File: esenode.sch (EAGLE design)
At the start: 11 parts, among them Q1 CSTCR6M00G53Z, U1 LPC11U6XJBD48, U2 RFM95W-868S2

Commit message: #challenge, then connect gpio to top bar and see if still possible lol
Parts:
- removed LD1: 67-23SDRSUGSUBC/TR8, everlight:67-23SDRSUGSUBC/TR8
- removed R3, R4: 10, eagle-ltspice:RR0603
- removed U2: RFM95W-868S2, RFM95W-868S2:RFM95W-868S2
- added C1: 1U, rcl:C-EUC0805
- added S1, S2: DTSM-6, switch-tact:DTSM-6
- added SV1, SV3: (no value), con-lstb:MA09-1
- added SV2: (no value), con-lstb:MA12-1
- R1: value 1U -> 10k; device resistor:R-EU_R0603 -> rcl:R-EU_M0805
- R2: value 56 -> 10k; device eagle-ltspice:RR0603 -> rcl:R-EU_M0805
- U1: value LPC11U6XJBD48 -> LPC11U68JBD64; device NXP_60_26022015:LPC11U6XJBD48 -> NXP_60_26022015:LPC11U68JBD64
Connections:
- net N$1 renamed XIN
- net N$2 renamed XOUT
- net N$3 renamed D-
- net N$4 renamed D+
- net N$5 renamed VIN
- removed net +3V3: LD1.CA, R1.1, U$2.VOUT, U$3.VCC, U1.VBAT, U1.VDD, U1.VDDA
- removed net BLUE: R4.1, U1.PIO2_7
- removed net GREEN: R3.1, U1.PIO2_2
- removed net N$8: LD1.BC, R4.2
- removed net RED: R2.1, U1.PIO1_13
- new net ANT: U$3.ANT
- new net INT0: U$3.DIO0, U1.PIO0_19
- new net ISP_ENTRY: S2.1, U1.PIO0_1
- new net N$18: SV3.3
- new net N$4: U1.VREFP
- new net NRESET: S1.1, SV3.2, U1.!RESET!/PIO0_0
- new net PWM0: SV1.6, U1.PIO1_19
- new net PWM02: SV3.9, U1.PIO2_18
- new net PWM03: SV3.8, U1.PIO2_19
- new net PWM1: SV1.7, U1.PIO2_2
- new net PWM2: SV1.8, U1.PIO2_7
- new net PWM3: SV1.9, U1.PIO1_13
- new net RX1: SV1.2, U1.TDO/PIO0_13
- new net SCL0: SV1.4, U1.PIO0_4
- new net SDA0: SV1.5, U1.PIO0_5
- new net TX1: SV1.3, U1.!TRST!/PIO0_14
- new net VCC: C1.2, R1.2, R2.2, SV1.1, U$2.VOUT, U$3.VCC, U1.PIO0_3, U1.VBAT, U1.VDD, U1.VDDA
- net GND: now also C1.1, S1.3, S1.4, S2.3, S2.4, SV3.1, U$3.GNDA, U$3.GNDB; no longer R1.2
- net MISO0: now also SV3.5
- net MOSI0: now also SV3.6
- net N$6: now also R2.1, S2.2; no longer LD1.RC, R2.2
- net N$7: now also R1.1, S1.2; no longer LD1.GC, R3.2
- net SCK0: now also SV3.4, U1.SWCLK/PIO0_10
- net SS0: now also SV3.7, U$3.NSS
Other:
- moved on the sheet: Q1, R1, R2, U$1, U$2

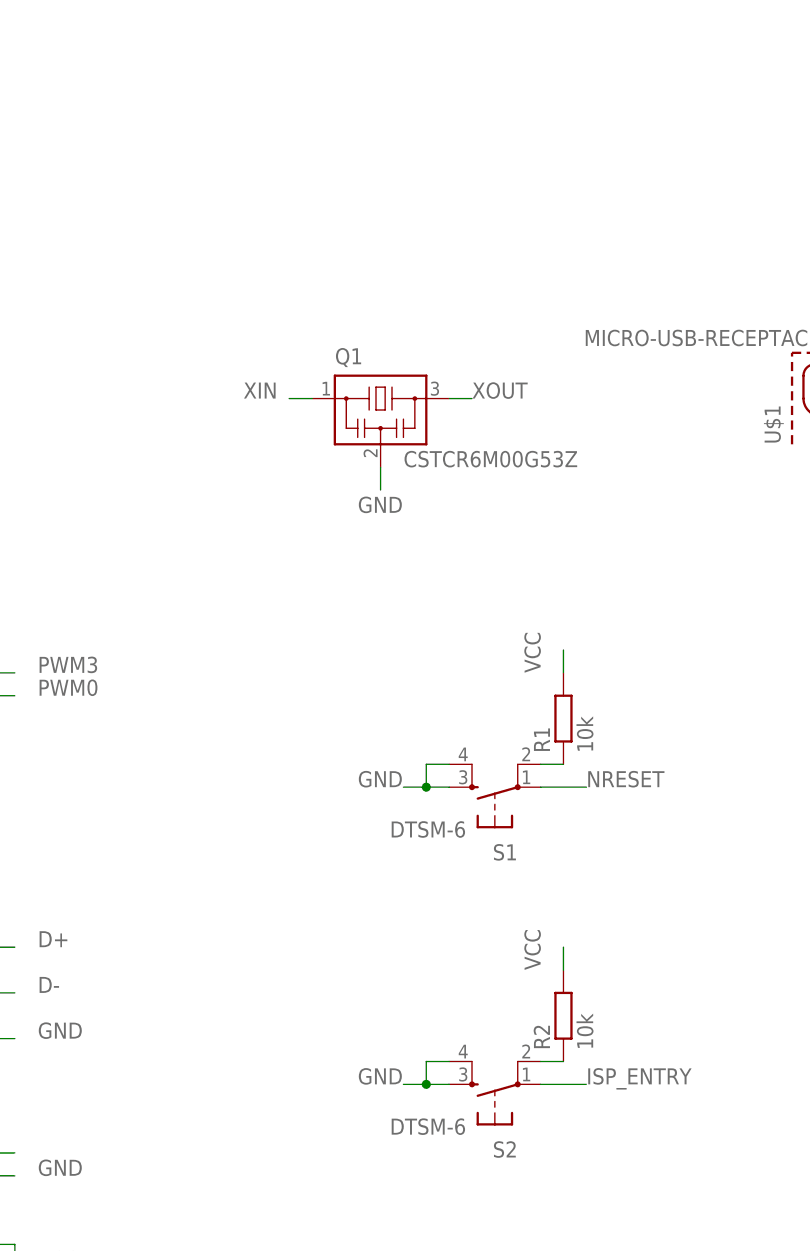
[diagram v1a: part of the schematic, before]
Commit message: added antenna
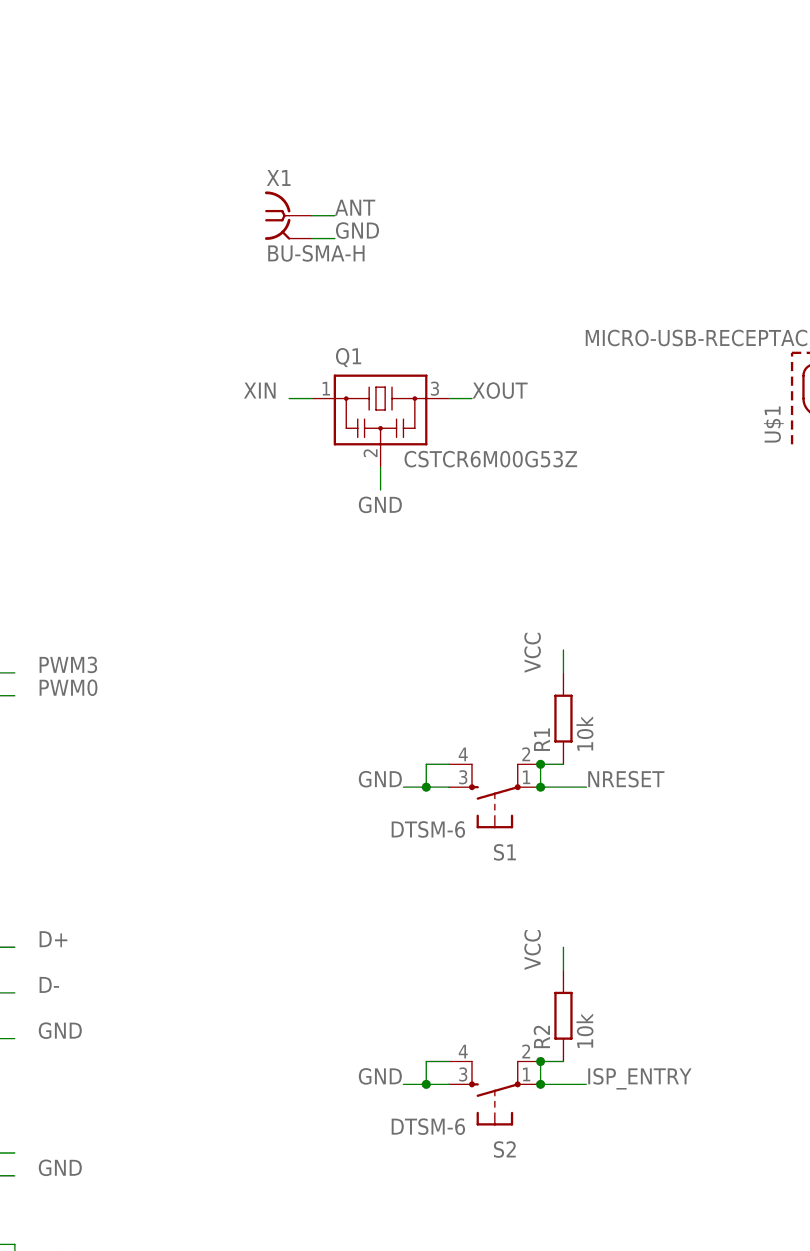
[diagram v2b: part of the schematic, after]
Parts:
- added X1: BU-SMA-H, con-coax:BU-SMA-H
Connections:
- removed net N$6: R2.1, S2.2
- removed net N$7: R1.1, S1.2
- net ANT: now also X1.1
- net GND: now also X1.2
- net ISP_ENTRY: now also R2.1, S2.2
- net NRESET: now also R1.1, S1.2
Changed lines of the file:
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@@
 <part name="SV2" library="con-lstb" deviceset="MA12-1" device=""/>
 <part name="U$3" library="hoperf" deviceset="RFM69HW" device=""/>
+<part name="X1" library="con-coax" deviceset="BU-SMA-H" device=""/>
 </parts>
 <sheets>
@@
 <instance part="SV2" gate="1" x="223.52" y="35.56"/>
 <instance part="U$3" gate="A" x="66.04" y="175.26"/>
+<instance part="X1" gate="G$1" x="160.02" y="147.32"/>
 </instances>
 <busses>
@@
 <wire x1="256.54" y1="66.04" x2="259.08" y2="66.04" width="0.1524" layer="91"/>
 <label x="259.08" y="66.04" size="1.778" layer="95"/>
+</segment>
+<segment>
+<pinref part="X1" gate="G$1" pin="2"/>
+<wire x1="162.56" y1="144.78" x2="165.1" y2="144.78" width="0.1524" layer="91"/>
+<label x="165.1" y="144.78" size="1.778" layer="95"/>
 </segment>
 </net>
@@
 <wire x1="187.96" y1="83.82" x2="193.04" y2="83.82" width="0.1524" layer="91"/>
 <label x="193.04" y="83.82" size="1.778" layer="95"/>
+<pinref part="S1" gate="G$1" pin="2"/>
+<pinref part="R1" gate="G$1" pin="1"/>
+<wire x1="187.96" y1="86.36" x2="190.5" y2="86.36" width="0.1524" layer="91"/>
+<wire x1="187.96" y1="83.82" x2="187.96" y2="86.36" width="0.1524" layer="91"/>
+<junction x="187.96" y="83.82"/>
+<junction x="187.96" y="86.36"/>
 </segment>
 <segment>
@@
 <wire x1="187.96" y1="50.8" x2="193.04" y2="50.8" width="0.1524" layer="91"/>
 <label x="193.04" y="50.8" size="1.778" layer="95"/>
-</segment>
-</net>
-<net name="N$6" class="0">
-<segment>
 <pinref part="S2" gate="G$1" pin="2"/>
 <pinref part="R2" gate="G$1" pin="1"/>
 <wire x1="187.96" y1="53.34" x2="190.5" y2="53.34" width="0.1524" layer="91"/>
-</segment>
-</net>
-<net name="N$7" class="0">
-<segment>
-<pinref part="S1" gate="G$1" pin="2"/>
-<pinref part="R1" gate="G$1" pin="1"/>
-<wire x1="187.96" y1="86.36" x2="190.5" y2="86.36" width="0.1524" layer="91"/>
+<wire x1="187.96" y1="50.8" x2="187.96" y2="53.34" width="0.1524" layer="91"/>
+<junction x="187.96" y="50.8"/>
+<junction x="187.96" y="53.34"/>
 </segment>
 </net>
@@
 <label x="91.44" y="149.86" size="1.778" layer="95"/>
 </segment>
-</net>
+<segment>
+<pinref part="X1" gate="G$1" pin="1"/>
+<wire x1="162.56" y1="147.32" x2="165.1" y2="147.32" width="0.1524" layer="91"/>
+<label x="165.1" y="147.32" size="1.778" layer="95"/>
+</segment>
+</net>
